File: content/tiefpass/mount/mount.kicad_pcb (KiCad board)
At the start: 2 copper layers, 40.3 x 108.2 mm, 15 parts, among them J1 IN, J2 CV1, J3 CV2, J4 CV, SW1 SWITCH_3PDT, SW2 SW_SPDT

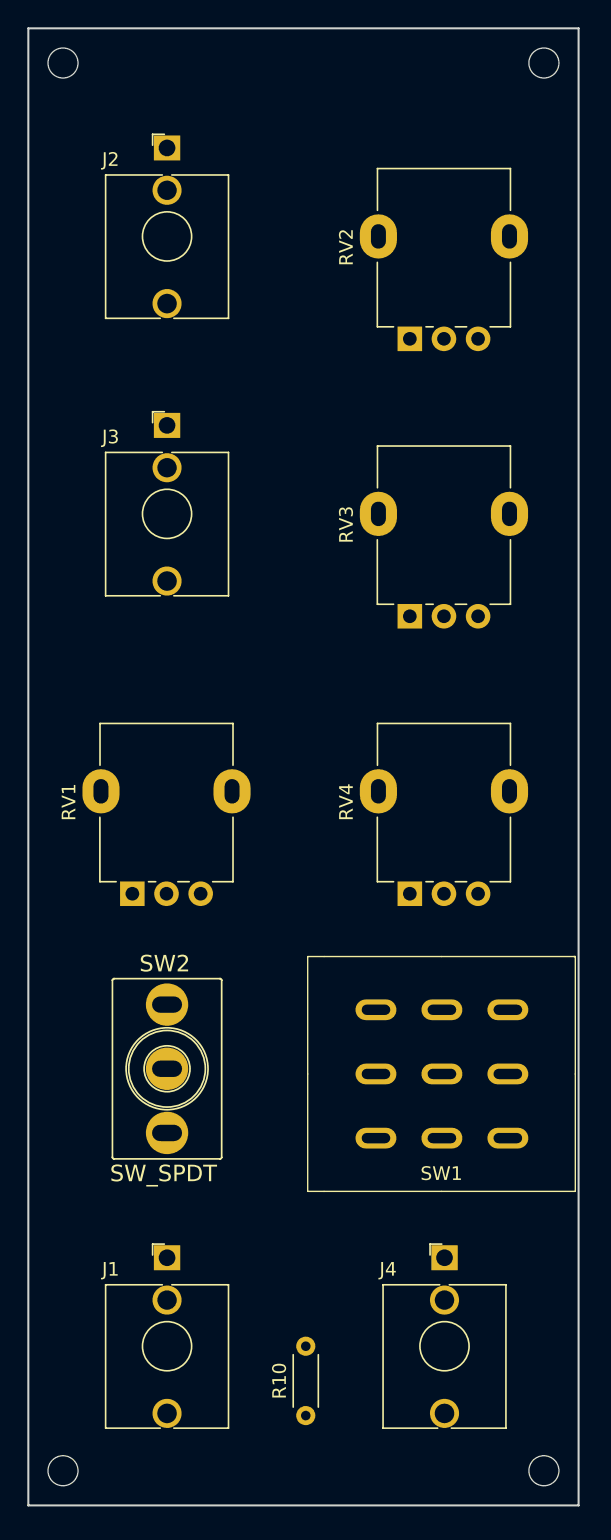
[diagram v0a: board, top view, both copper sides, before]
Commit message: tiefpass add panel
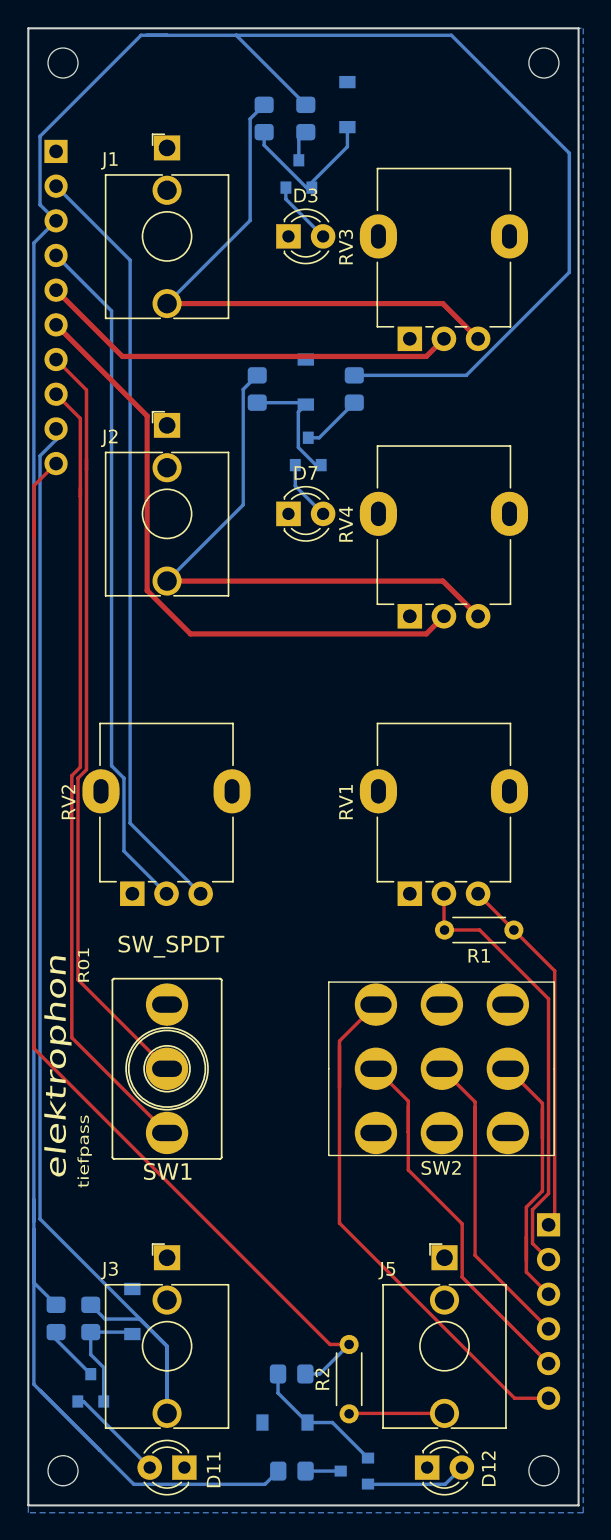
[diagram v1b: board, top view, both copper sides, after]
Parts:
- removed the RV4 at (81.3, 106.7)
- added D1: 1N4148W, Diode_SMD:D_SOD-123, B.Cu at (74.2, 56.4)
- added D10: 1N4148W, Diode_SMD:D_SOD-123, B.Cu at (69.6, 152.9)
- added D11: LED (Green), LED_THT:LED_D3.0mm, F.Cu at (62.2, 156.2)
- added D12: LED (Red), LED_THT:LED_D3.0mm, F.Cu at (80.0, 156.2)
- added D3: LED (Yellow), LED_THT:LED_D3.0mm, F.Cu at (69.8, 66.0)
- added D5: 1N4148W, Diode_SMD:D_SOD-123, B.Cu at (71.1, 76.7)
- added D7: LED (Yellow), LED_THT:LED_D3.0mm, F.Cu at (69.8, 86.4)
- added D9: 1N4148W, Diode_SMD:D_SOD-123, B.Cu at (58.4, 144.8)
- added J4: Conn_01x10_Male, Connector_PinSocket_2.54mm:PinSocket_1x10_P2.54mm_Vertical, B.Cu at (52.8, 59.8)
- added J6: Conn_01x06_Male, Connector_PinSocket_2.54mm:PinSocket_1x06_P2.54mm_Vertical, B.Cu at (88.9, 138.4)
- added Q1: MMBT3904, Package_TO_SOT_SMD:SOT-23, B.Cu at (70.6, 61.5)
- added Q3: MMBT3904, Package_TO_SOT_SMD:SOT-23, B.Cu at (71.3, 81.8)
- added Q5: MMBT3904, Package_TO_SOT_SMD:SOT-23, B.Cu at (55.4, 150.4)
- added Q6: MMBT3904, Package_TO_SOT_SMD:SOT-23, B.Cu at (74.7, 156.5)
- added R1: 22k, Resistor_THT:R_Axial_DIN0204_L3.6mm_D1.6mm_P5.08mm_Horizontal, F.Cu at (86.4, 116.8)
- added R11: 100k, Resistor_SMD:R_0805_2012Metric_Pad1.20x1.40mm_HandSolder, B.Cu at (55.4, 145.3)
- added R12: 100k, Resistor_SMD:R_0805_2012Metric_Pad1.20x1.40mm_HandSolder, B.Cu at (70.1, 149.4)
- added R13: 5k, Resistor_SMD:R_0805_2012Metric_Pad1.20x1.40mm_HandSolder, B.Cu at (52.8, 145.3)
- added R14: 5k, Resistor_SMD:R_0805_2012Metric_Pad1.20x1.40mm_HandSolder, B.Cu at (70.1, 156.5)
- added R3: 100k, Resistor_SMD:R_0805_2012Metric_Pad1.20x1.40mm_HandSolder, B.Cu at (68.1, 57.4)
- added R5: 5k, Resistor_SMD:R_0805_2012Metric_Pad1.20x1.40mm_HandSolder, B.Cu at (71.1, 57.4)
- added R7: 100k, Resistor_SMD:R_0805_2012Metric_Pad1.20x1.40mm_HandSolder, B.Cu at (67.6, 77.2)
- added R9: 5k, Resistor_SMD:R_0805_2012Metric_Pad1.20x1.40mm_HandSolder, B.Cu at (74.7, 77.2)
- added REF**: elektrophon logo, elektrophon:elektrophon logo, F.Cu at (53.9, 126.9)
- added RV1: 100k, elektrophon:Potentiometer_Alpha_RD901F-40-00D_Single_Vertical, F.Cu at (81.3, 106.7)
- J5: renamed from J4; value CV -> OUT
- moved R2 3.18 mm to (74.3, 152.3)
- moved SW2 0.38 mm to (81.1, 127.0)
- turned SW1 to 180 degrees
- renumbered J2 to J1, J3 to J2, J1 to J3, R10 to R2, RV1 to RV2, RV2 to RV3, RV3 to RV4, SW2 to SW1, SW1 to SW2
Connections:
- net Net-(J2-PadT) renamed /CV_1
- net Net-(J3-PadT) renamed /CV_2
- J3 pad S: Net-(J1-PadS) -> GND
- J3 pad T: Net-(J1-PadT) -> IN
- R2 pad 2: Net-(R10-Pad2) -> OUT
- RV2 pad 2: Net-(RV1-Pad2) -> CV
- RV3 pad 2: Net-(RV2-Pad2) -> CV1
- RV4 pad 2: Net-(RV3-Pad2) -> CV2
- SW1 pad 1: Net-(SW2-Pad1) -> /S2b
- SW1 pad 2: Net-(SW2-Pad2) -> /S2a
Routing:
- net +5V: track 0.00 -> 209.6 mm
- net IN: track 0.00 -> 88.2 mm
- net OUT: track 0.00 -> 80.8 mm
- net /S2b: track 0.00 -> 58.6 mm
- net /S2a: track 0.00 -> 56.6 mm
- net +15V: track 0.00 -> 56.2 mm
- net CV: track 0.00 -> 50.1 mm
- net CV2: track 0.00 -> 45.8 mm
- net /CV_2: track 0.00 -> 41.6 mm
- net /CV_1: track 0.00 -> 41.4 mm
- net /S4: track 0.00 -> 40.7 mm
- net RES_1_out: track 0.00 -> 32.4 mm
- net CV1: track 0.00 -> 31.0 mm
- net /S3: track 0.00 -> 28.7 mm
- net RES_1: track 0.00 -> 26.8 mm
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- added copper zone on B.Cu, net GND
